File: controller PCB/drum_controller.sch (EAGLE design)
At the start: 1 part

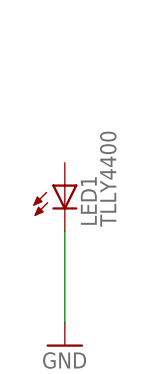
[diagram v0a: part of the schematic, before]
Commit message: connected LED anode to +5V
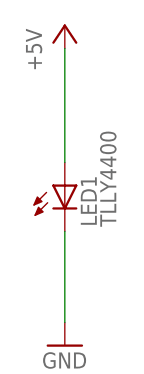
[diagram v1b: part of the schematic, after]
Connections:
- new net +5V: LED1.A
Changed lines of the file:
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@@
 <part name="LED1" library="led" deviceset="TLLY4400" device=""/>
 <part name="GND1" library="supply1" deviceset="GND" device=""/>
+<part name="P+1" library="supply1" deviceset="+5V" device=""/>
 </parts>
 <sheets>
@@
 <instance part="LED1" gate="G$1" x="38.1" y="73.66"/>
 <instance part="GND1" gate="1" x="38.1" y="55.88"/>
+<instance part="P+1" gate="1" x="38.1" y="91.44"/>
 </instances>
 <busses>
@@
 </segment>
 </net>
+<net name="+5V" class="0">
+<segment>
+<pinref part="LED1" gate="G$1" pin="A"/>
+<pinref part="P+1" gate="1" pin="+5V"/>
+<wire x1="38.1" y1="76.2" x2="38.1" y2="88.9" width="0.1524" layer="91"/>
+</segment>
+</net>

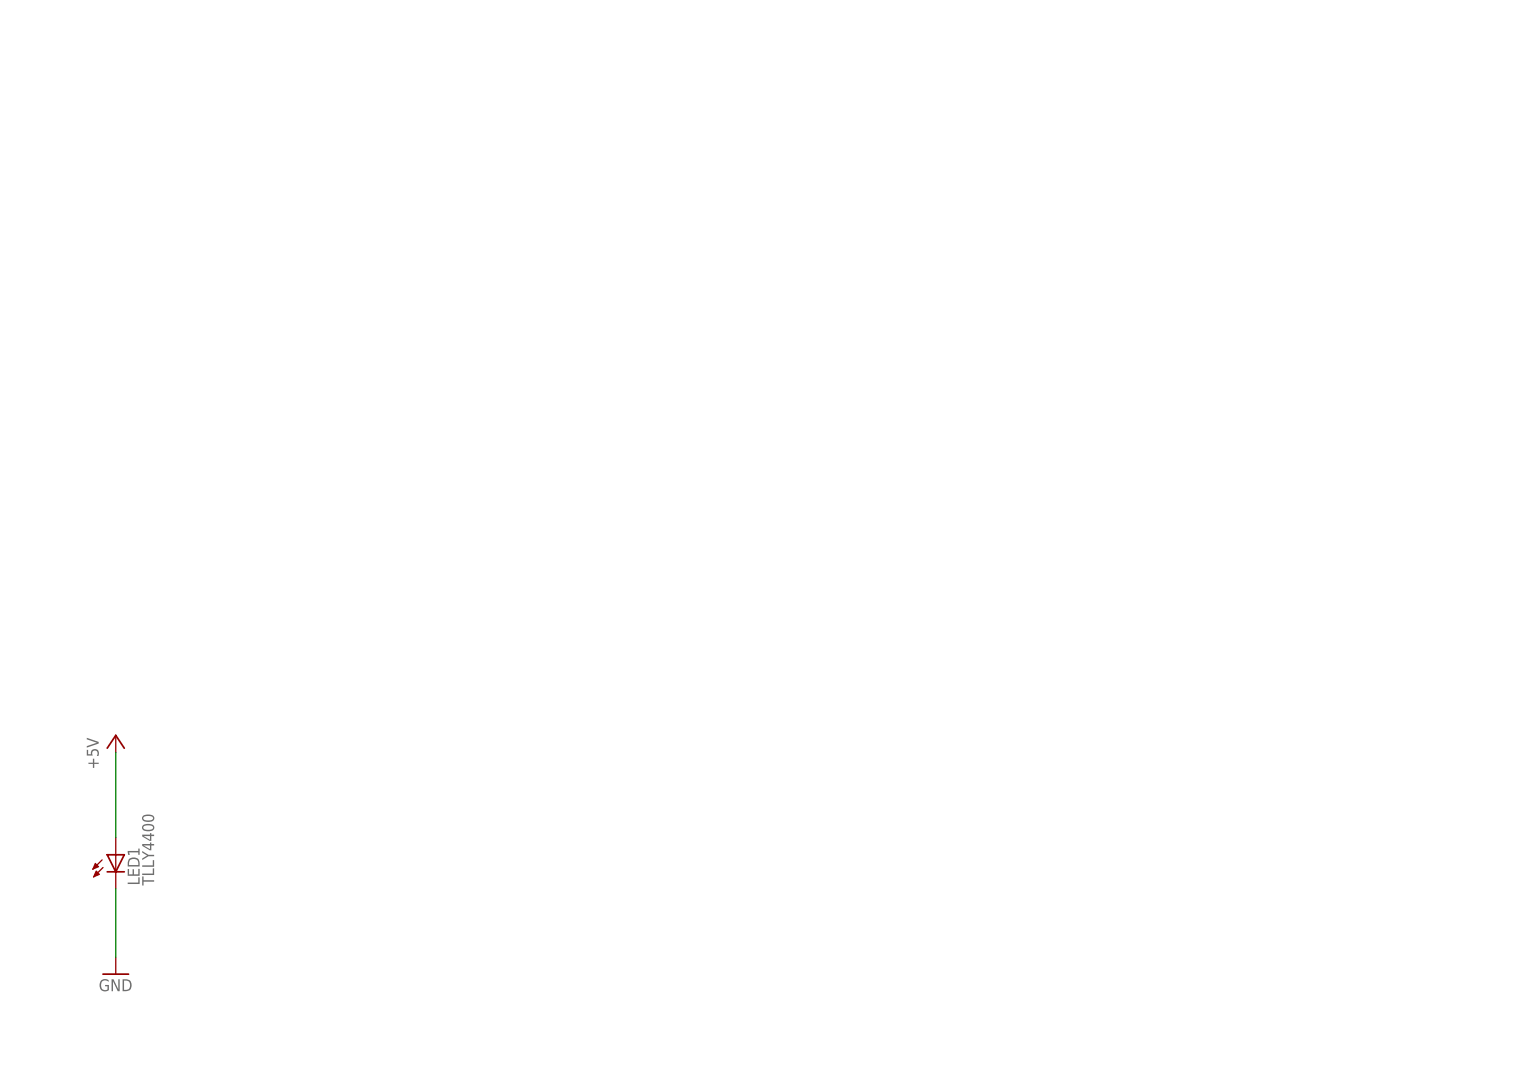
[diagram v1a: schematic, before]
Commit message: added all 8 piezos to schematic, board not layed out yet
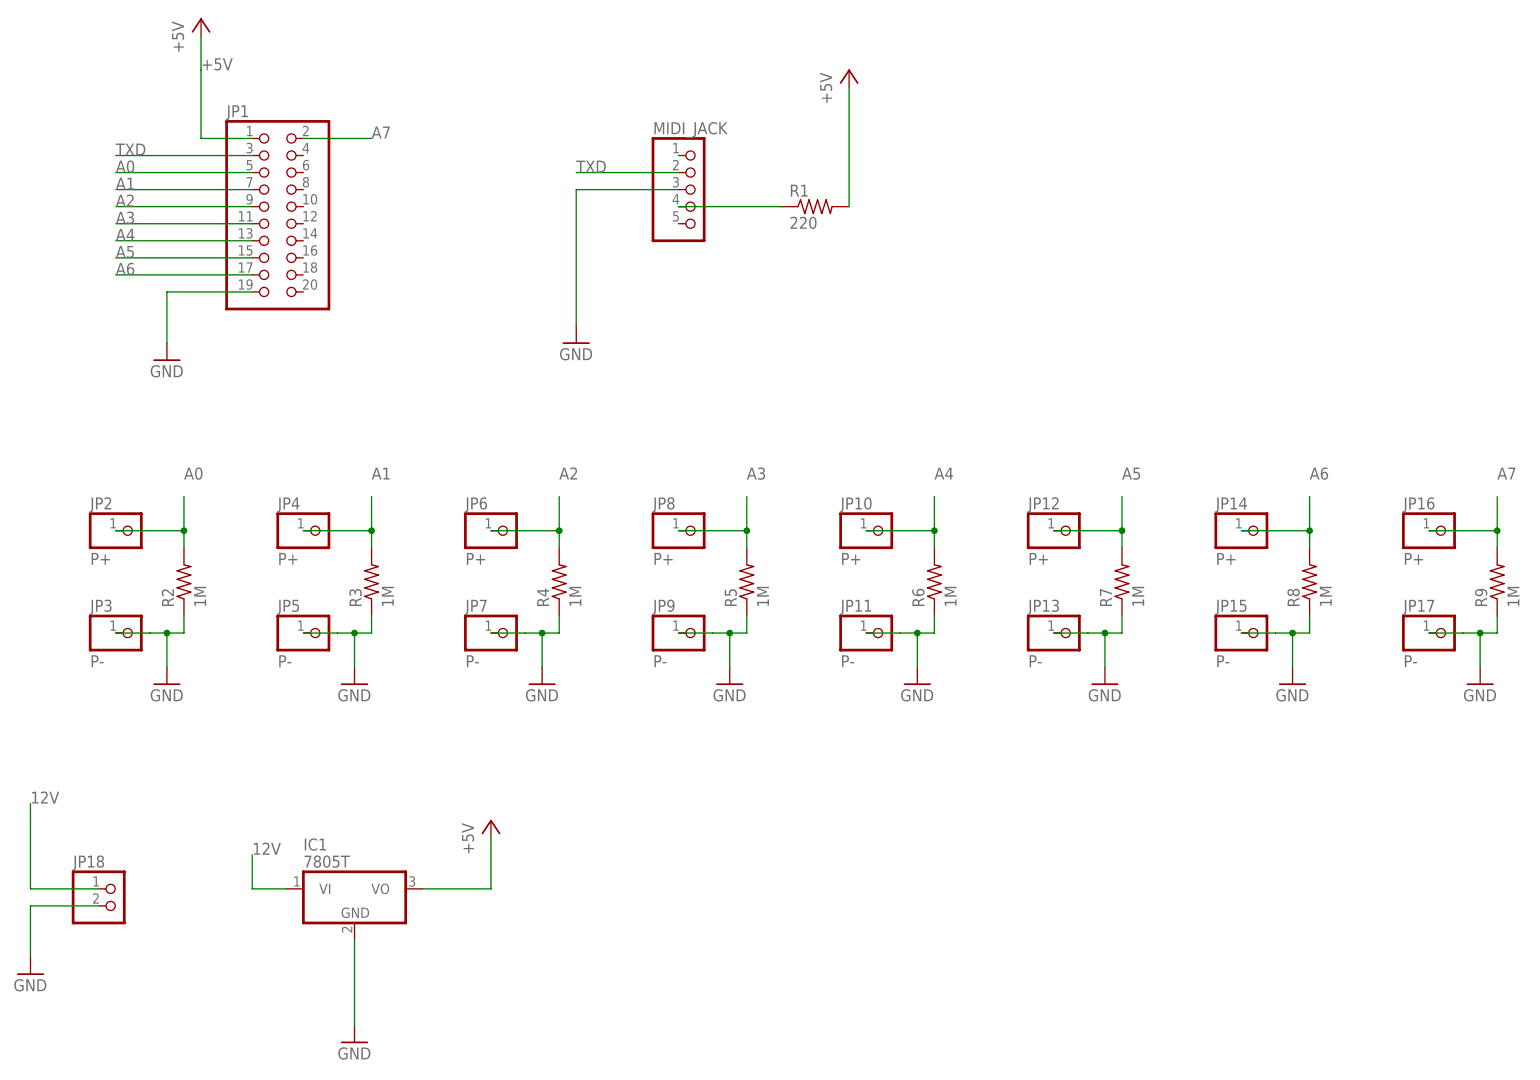
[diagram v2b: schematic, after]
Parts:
- removed LED1: TLLY4400, led:TLLY4400
- added IC1: 7805T, adafruit:7805T
- added JP1: (no value), pinhead:PINHD-2X10
- added JP10, JP12, JP14, JP16, JP2, JP4, JP6, JP8: P+, pinhead:PINHD-1X1
- added JP11, JP13, JP15, JP17, JP3, JP5, JP7, JP9: P-, pinhead:PINHD-1X1
- added JP18: (no value), pinhead:PINHD-1X2
- added MIDI_JACK: (no value), pinhead:PINHD-1X5
- added R1: 220, rcl:R-US_0817/22
- added R2, R3, R4, R5, R6, R7, R8, R9: 1M, rcl:R-US_0817/22
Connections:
- new net 12V: IC1.VI, JP18.1
- new net A0: JP1.5, JP2.1, R2.2
- new net A1: JP1.7, JP4.1, R3.2
- new net A2: JP1.9, JP6.1, R4.2
- new net A3: JP1.11, JP8.1, R5.2
- new net A4: JP1.13, JP10.1, R6.2
- new net A5: JP1.15, JP12.1, R7.2
- new net A6: JP1.17, JP14.1, R8.2
- new net A7: JP1.2, JP16.1, R9.2
- new net N$1: MIDI_JACK.4, R1.1
- new net TXD: JP1.3, MIDI_JACK.2
- net +5V: now also IC1.VO, JP1.1, R1.2; no longer LED1.A
- net GND: now also IC1.GND, JP1.19, JP11.1, JP13.1, JP15.1, JP17.1, JP18.2, JP3.1, JP5.1, JP7.1, JP9.1, MIDI_JACK.3, R2.1, R3.1, R4.1, R5.1, R6.1, R7.1, R8.1, R9.1; no longer LED1.C

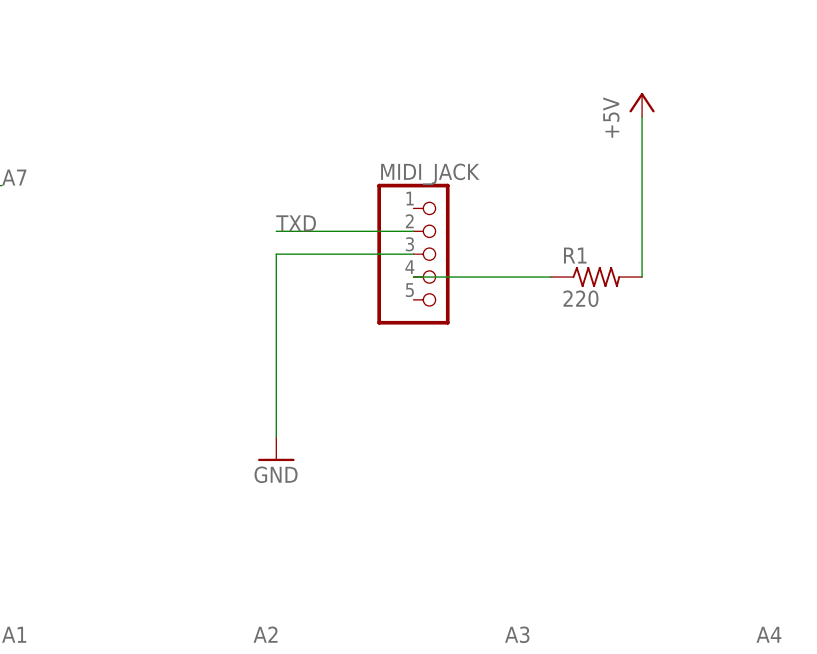
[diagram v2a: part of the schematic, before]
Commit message: added proper MIDI jack from external library; added lower enclosure notch (will add matching notch with Zoe)
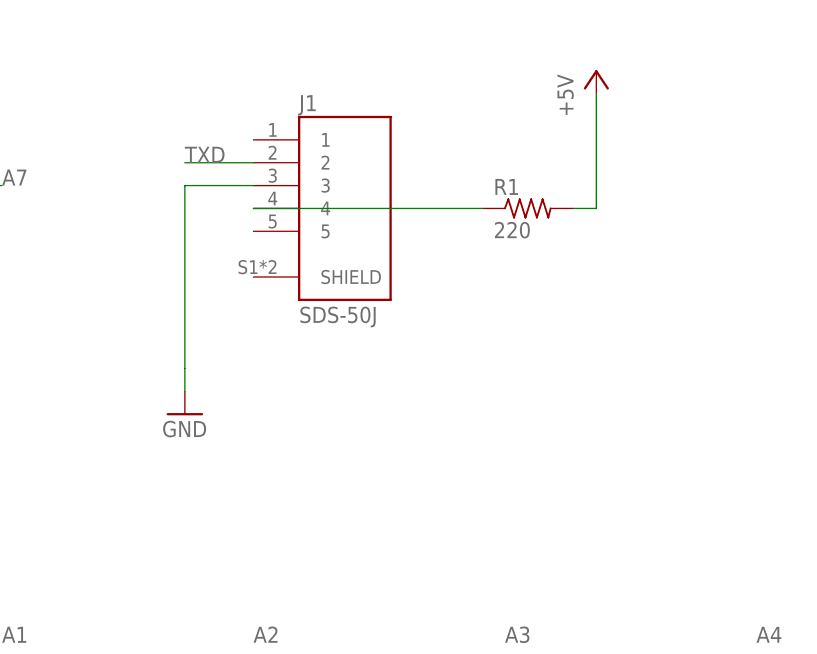
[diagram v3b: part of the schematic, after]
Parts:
- removed MIDI_JACK: (no value), pinhead:PINHD-1X5
- added J1: SDS-50J, SDS-50J:SDS-50J
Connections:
- net GND: now also J1.3; no longer MIDI_JACK.3
- net N$1: now also J1.4; no longer MIDI_JACK.4
- net TXD: now also J1.2; no longer MIDI_JACK.2
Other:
- moved on the sheet: R1
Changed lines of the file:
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@@
 <part name="P+1" library="supply1" deviceset="+5V" device=""/>
 <part name="GND1" library="supply1" deviceset="GND" device=""/>
-<part name="MIDI_JACK" library="pinhead" deviceset="PINHD-1X5" device=""/>
-<part name="P+2" library="supply1" deviceset="+5V" device=""/>
 <part name="R1" library="rcl" deviceset="R-US_" device="0817/22" value="220"/>
-<part name="GND2" library="supply1" deviceset="GND" device=""/>
 <part name="JP2" library="pinhead" deviceset="PINHD-1X1" device="" value="P+"/>
 <part name="JP3" library="pinhead" deviceset="PINHD-1X1" device="" value="P-"/>
@@
 <part name="GND12" library="supply1" deviceset="GND" device=""/>
 <part name="P+3" library="supply1" deviceset="+5V" device=""/>
+<part name="J1" library="SDS-50J" deviceset="SDS-50J" device=""/>
+<part name="P+4" library="supply1" deviceset="+5V" device=""/>
+<part name="GND13" library="supply1" deviceset="GND" device=""/>
 </parts>
 <sheets>
@@
 <instance part="P+1" gate="1" x="50.8" y="198.12"/>
 <instance part="GND1" gate="1" x="45.72" y="147.32"/>
-<instance part="MIDI_JACK" gate="A" x="124.46" y="172.72"/>
-<instance part="P+2" gate="1" x="147.32" y="190.5"/>
-<instance part="R1" gate="G$1" x="142.24" y="170.18"/>
-<instance part="GND2" gate="1" x="106.68" y="149.86"/>
+<instance part="R1" gate="G$1" x="134.62" y="177.8"/>
 <instance part="JP2" gate="G$1" x="40.64" y="121.92"/>
 <instance part="JP3" gate="G$1" x="40.64" y="106.68"/>
@@
 <instance part="GND12" gate="1" x="73.66" y="45.72"/>
 <instance part="P+3" gate="1" x="93.98" y="78.74"/>
+<instance part="J1" gate="G$1" x="114.3" y="177.8"/>
+<instance part="P+4" gate="1" x="142.24" y="193.04"/>
+<instance part="GND13" gate="1" x="96.52" y="154.94"/>
 </instances>
 <busses>
@@
 </segment>
 <segment>
-<pinref part="R1" gate="G$1" pin="2"/>
-<pinref part="P+2" gate="1" pin="+5V"/>
-<wire x1="147.32" y1="170.18" x2="147.32" y2="187.96" width="0.1524" layer="91"/>
-</segment>
-<segment>
 <pinref part="IC1" gate="A1" pin="VO"/>
 <wire x1="83.82" y1="68.58" x2="93.98" y2="68.58" width="0.1524" layer="91"/>
@@
 <wire x1="93.98" y1="68.58" x2="93.98" y2="76.2" width="0.1524" layer="91"/>
 </segment>
+<segment>
+<pinref part="R1" gate="G$1" pin="2"/>
+<pinref part="P+4" gate="1" pin="+5V"/>
+<wire x1="139.7" y1="177.8" x2="142.24" y2="177.8" width="0.1524" layer="91"/>
+<wire x1="142.24" y1="177.8" x2="142.24" y2="190.5" width="0.1524" layer="91"/>
+</segment>
 </net>
 <net name="GND" class="0">
@@
 <wire x1="58.42" y1="157.48" x2="45.72" y2="157.48" width="0.1524" layer="91"/>
 <wire x1="45.72" y1="157.48" x2="45.72" y2="149.86" width="0.1524" layer="91"/>
-</segment>
-<segment>
-<pinref part="MIDI_JACK" gate="A" pin="3"/>
-<pinref part="GND2" gate="1" pin="GND"/>
-<wire x1="121.92" y1="172.72" x2="106.68" y2="172.72" width="0.1524" layer="91"/>
-<wire x1="106.68" y1="172.72" x2="106.68" y2="152.4" width="0.1524" layer="91"/>
 </segment>
 <segment>
@@
 <wire x1="73.66" y1="48.26" x2="73.66" y2="60.96" width="0.1524" layer="91"/>
 </segment>
-</net>
-<net name="N$1" class="0">
-<segment>
-<pinref part="R1" gate="G$1" pin="1"/>
-<wire x1="121.92" y1="170.18" x2="137.16" y2="170.18" width="0.1524" layer="91"/>
-<pinref part="MIDI_JACK" gate="A" pin="4"/>
+<segment>
+<pinref part="J1" gate="G$1" pin="3"/>
+<wire x1="104.14" y1="180.34" x2="96.52" y2="180.34" width="0.1524" layer="91"/>
+<wire x1="96.52" y1="180.34" x2="96.52" y2="160.02" width="0.1524" layer="91"/>
+<pinref part="GND13" gate="1" pin="GND"/>
+<wire x1="96.52" y1="160.02" x2="96.52" y2="157.48" width="0.1524" layer="91"/>
 </segment>
 </net>
@@
 </segment>
 <segment>
-<pinref part="MIDI_JACK" gate="A" pin="2"/>
-<wire x1="121.92" y1="175.26" x2="106.68" y2="175.26" width="0.1524" layer="91"/>
-<label x="106.68" y="175.26" size="1.778" layer="95"/>
+<pinref part="J1" gate="G$1" pin="2"/>
+<wire x1="104.14" y1="182.88" x2="96.52" y2="182.88" width="0.1524" layer="91"/>
+<label x="96.52" y="182.88" size="1.778" layer="95"/>
 </segment>
 </net>
@@
 </segment>
 </net>
+<net name="N$1" class="0">
+<segment>
+<pinref part="J1" gate="G$1" pin="4"/>
+<wire x1="104.14" y1="177.8" x2="129.54" y2="177.8" width="0.1524" layer="91"/>
+<pinref part="R1" gate="G$1" pin="1"/>
+</segment>
+</net>
